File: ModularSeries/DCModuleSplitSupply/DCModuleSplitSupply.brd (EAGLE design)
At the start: 81.3 x 36.5 mm, 21 parts, among them J1 2XMOLEX, J2 4XMOLEX, J3 4XMOLEX, J4 4XMOLEX, J5 4XMOLEX, J6 2XMOLEX, J7 2XMOLEX, J8 4XMOLEX

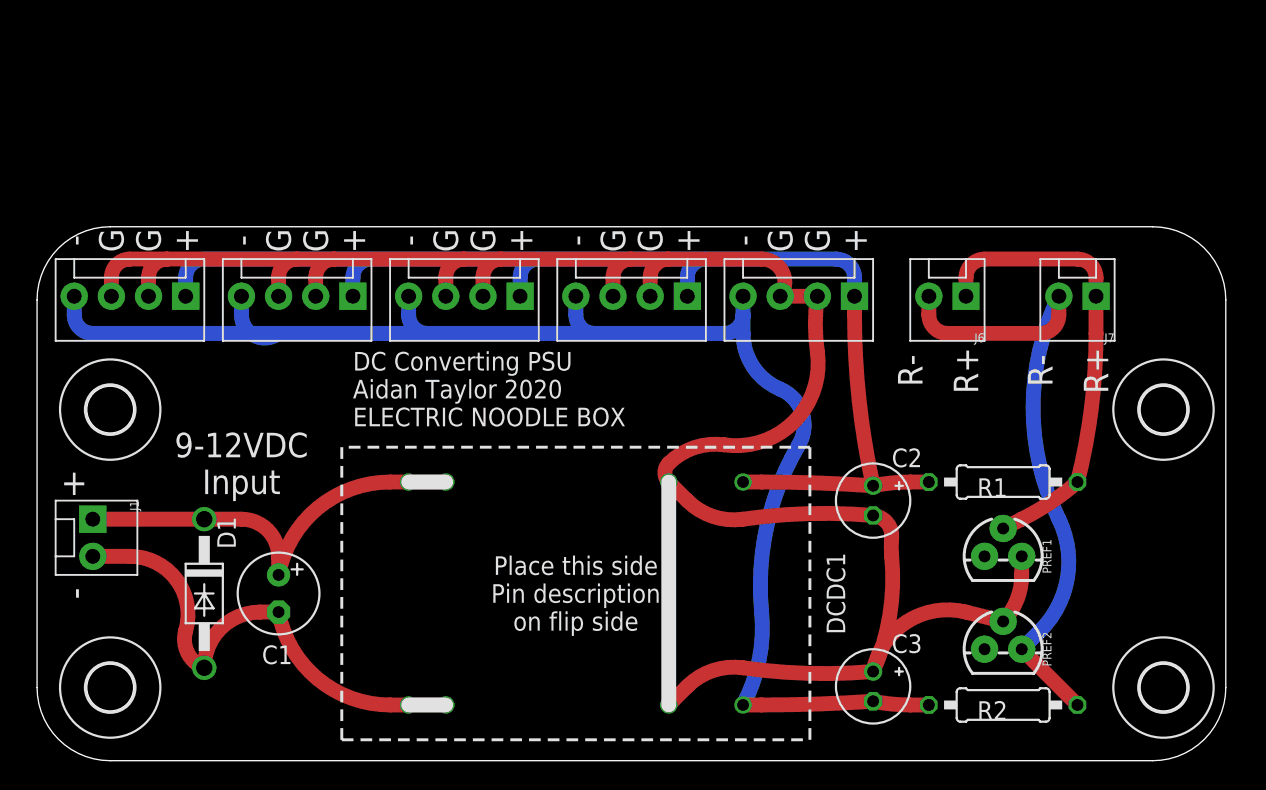
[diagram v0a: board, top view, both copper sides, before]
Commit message: Updates to Prism, VCA, PSU and Prism BOM added
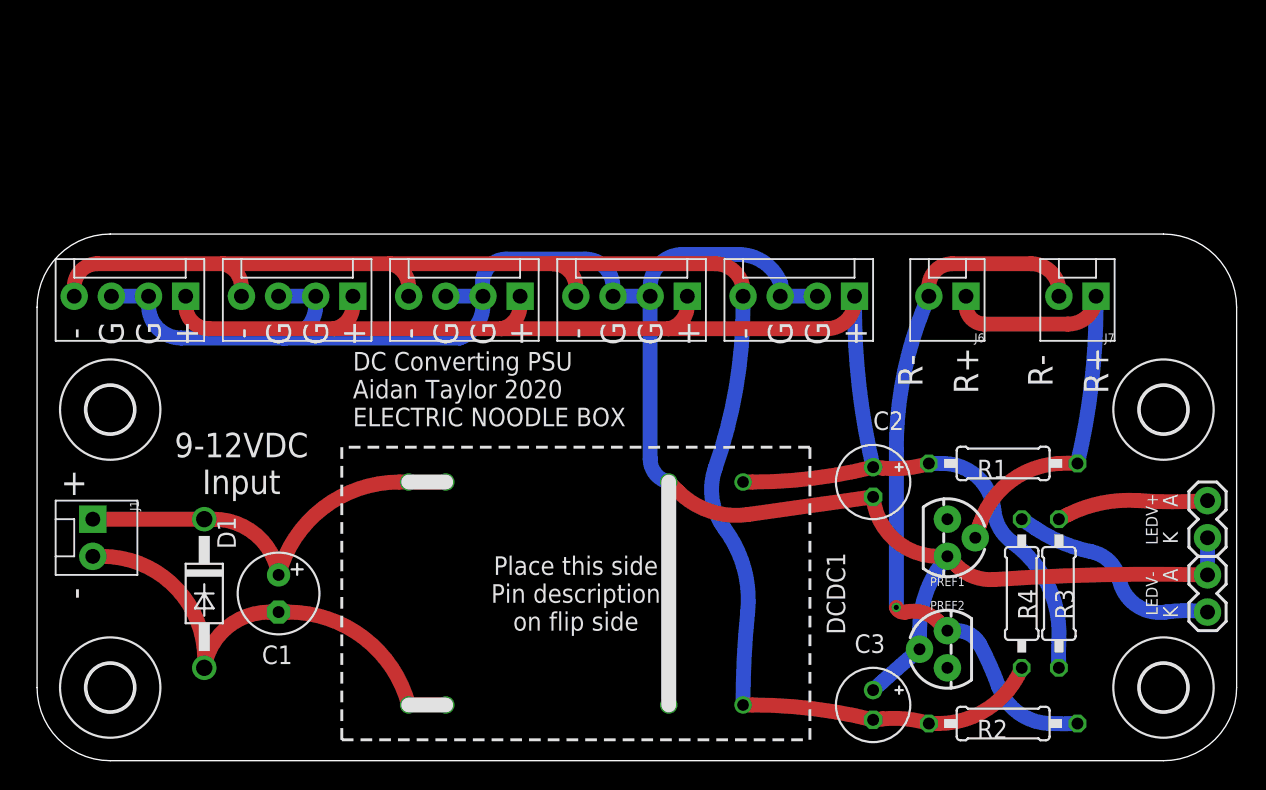
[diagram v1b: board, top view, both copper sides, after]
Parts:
- added LEDV+, LEDV-: 2XWIREPAD, ElectricNoodleBox:1X02
- added R3, R4: 1K, rcl:0207/10
- moved PREF1 4.02 mm to (62.2, 15.2), turned to 270 degrees
- moved PREF2 3.81 mm to (62.2, 7.62), turned to 90 degrees
- moved C3 1.27 mm to (57.1, 3.81)
- moved R2 1.27 mm to (66.0, 2.54)
- moved C2 1.27 mm to (57.1, 19.1)
- moved R1 1.27 mm to (66.0, 20.3)
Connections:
- new net N$2: LEDV+.2, R3.1
- new net N$3: LEDV-.2, R4.1
- net +12V: now also R3.2
- net -12V: now also R4.2
- net AGND: now also LEDV+.1, LEDV-.1
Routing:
- net N$3: track 0.00 -> 14.7 mm
- net +12V: track 84.2 -> 98.1 mm
- net N$2: track 0.00 -> 10.3 mm
- net -10VREF: track 42.6 -> 48.5 mm, vias 0 -> 1
- net -12V: track 100.3 -> 104.9 mm
- net AGND: track 146.7 -> 147.8 mm
- net N$5: track 32.1 -> 31.1 mm
- net N$4: track 28.8 -> 27.7 mm
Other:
- board size 81.3 x 36.5 mm -> 82 x 36 mm
- board text added: "A"
- board text added: "K"

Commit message: Portals files updated, schematic exports and images included
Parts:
- added LINK: 2XWIREPAD, ElectricNoodleBox:1X02
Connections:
- net AGND: now also LINK.1, LINK.2
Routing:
- net AGND: track 147.8 -> 177.5 mm
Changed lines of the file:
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@@
 <attribute name="VALUE" x="66.675" y="13.6906" size="1.27" layer="27" ratio="10" rot="R270"/>
+</element>
+<element name="LINK" library="ElectricNoodleBox" package="1X02" value="2XWIREPAD" x="13.6525" y="2.8575" smashed="yes">
+<attribute name="NAME" x="11.6205" y="2.8575" size="0.8128" layer="25" font="vector" ratio="20" rot="R90" align="center"/>
+<attribute name="VALUE" x="13.6525" y="4.6355" size="0.6096" layer="27" font="vector" ratio="20"/>
 </element>
 </elements>
@@
 <wire x1="65.405" y1="12.3825" x2="80.01" y2="12.7" width="1.016" layer="1" curve="-5.285115"/>
 <wire x1="80.01" y1="15.24" x2="80.01" y2="12.7" width="1.016" layer="16"/>
+<contactref element="LINK" pad="1"/>
+<contactref element="LINK" pad="2"/>
+<wire x1="16.1925" y1="2.8575" x2="18.0975" y2="2.54" width="1.016" layer="1"/>
+<wire x1="18.0975" y1="2.54" x2="28.2575" y2="1.905" width="1.016" layer="1" curve="11.771976"/>
+<wire x1="28.2575" y1="1.905" x2="43.18" y2="3.81" width="1.016" layer="1" curve="9.930721"/>
+<wire x1="16.1925" y1="2.8575" x2="13.6525" y2="2.8575" width="1.016" layer="1"/>
 </signal>
 <signal name="N$2">

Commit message: DC Split Supply layout revision
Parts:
- removed J1, J6, J7: 2XMOLEX, ElectricNoodleBox:MOLEX-1X2
- removed J2, J3, J4, J5, J8: 4XMOLEX, ElectricNoodleBox:MOLEX-1X4
- added P1, P2, P3, P4, P5, P6: 4XMOLEX, ElectricNoodleBox:MOLEX-1X4
- added VIN, VREF1, VREF2: 2XMOLEX, ElectricNoodleBox:MOLEX-1X2
- moved H4 75.0 mm to (5.00, 45.0)
- moved R3 53.4 mm to (21.6, 34.3), turned to 180 degrees
- moved R1 51.2 mm to (15.2, 26.7), turned to 270 degrees
- moved H3 49.4 mm to (48.0, 45.0)
- moved C2 47.6 mm to (10.2, 26.7)
- moved H2 43.0 mm to (48.0, 5.00)
- moved R4 40.2 mm to (34.3, 34.3), turned to 0 degrees
- moved R2 35.0 mm to (40.6, 26.7), turned to 270 degrees
- moved LEDV+ 33.2 mm to (50.5, 30.5)
- moved LEDV- 33.2 mm to (50.5, 27.9)
- moved C3 25.6 mm to (45.7, 26.7), turned to 90 degrees
- moved LINK 22.9 mm to (2.54, 22.9), turned to 90 degrees
- moved PREF2 22.7 mm to (41.9, 17.8), turned to 180 degrees
- moved PREF1 20.7 mm to (41.9, 11.4), turned to 180 degrees
- moved H1 19.0 mm to (5.00, 5.00)
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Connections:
- net +10VREF: now also VREF1.1, VREF2.1; no longer J6.1, J7.1
- net +12V: now also P1.1, P2.1, P3.1, P4.1, P5.1, P6.1; no longer J2.1, J3.1, J4.1, J5.1, J8.1
- net -10VREF: now also VREF1.2, VREF2.2; no longer J6.2, J7.2
- net -12V: now also P1.4, P2.4, P3.4, P4.4, P5.4, P6.4; no longer J2.4, J3.4, J4.4, J5.4, J8.4
- net AGND: now also P1.2, P1.3, P2.2, P2.3, P3.2, P3.3, P4.2, P4.3, P5.2, P5.3, P6.2, P6.3; no longer J2.2, J2.3, J3.2, J3.3, J4.2, J4.3, J5.2, J5.3, J8.2, J8.3
- net N$4: now also VIN.1; no longer J1.1
- net N$5: now also VIN.2; no longer J1.2
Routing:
- net -12V: track 104.9 -> 71.0 mm, vias 0 -> 3
- net +12V: track 98.1 -> 70.9 mm, vias 0 -> 3
- net +10VREF: track 31.4 -> 53.2 mm, vias 0 -> 1
- net -10VREF: track 48.5 -> 28.0 mm
- net N$5: track 31.1 -> 48.8 mm, vias 0 -> 1
- net N$2: track 10.3 -> 24.7 mm
- net AGND: track 177.5 -> 166.6 mm, vias 0 -> 1
- net N$3: track 14.7 -> 24.8 mm, vias 0 -> 1
- net N$4: track 27.7 -> 36.1 mm, vias 0 -> 1
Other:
- board size 82 x 36 mm -> 53 x 50 mm
- board text added: "9V-12V in"
- board text added: "Aidan Taylor 2020"
- board text added: "DC to Split Supply"
- board text added: "ELECTRIC NOODLE BOX"
- board text added: "GND"
- board text added: "Ground Link"
- board text removed: "9-12VDC Input"
- board text removed: "DC Converting PSU Aidan Taylor 2020 ELECTRIC NOODLE BOX"
- board text removed: "G"
- board text removed: "R+"
- board text removed: "R-"
